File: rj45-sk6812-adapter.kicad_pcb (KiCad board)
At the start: 2 copper layers, 34.3 x 46.2 mm, 21 parts, among them J1 TE-Connectivity-406549-6, J2 Conn_01x05, J3 Conn_01x03, J4 Conn_01x03, J5 Conn_01x03, J6 Conn_01x03, J7 USB_B_Mini, J8 Screw_Terminal_01x02, Q1 2N7002, U1 L78L05_TO92

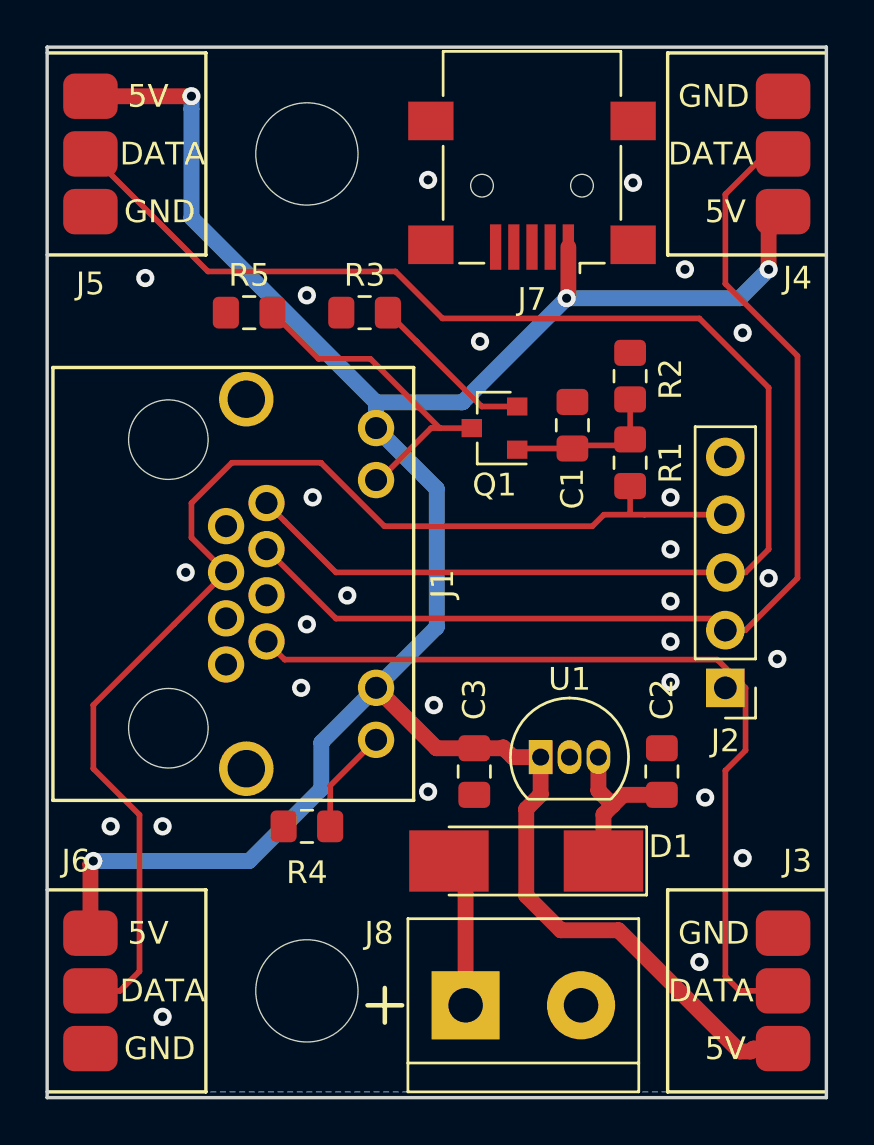
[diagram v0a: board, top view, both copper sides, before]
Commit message: Added capacitor to stabilize the LEDs' 5V supply
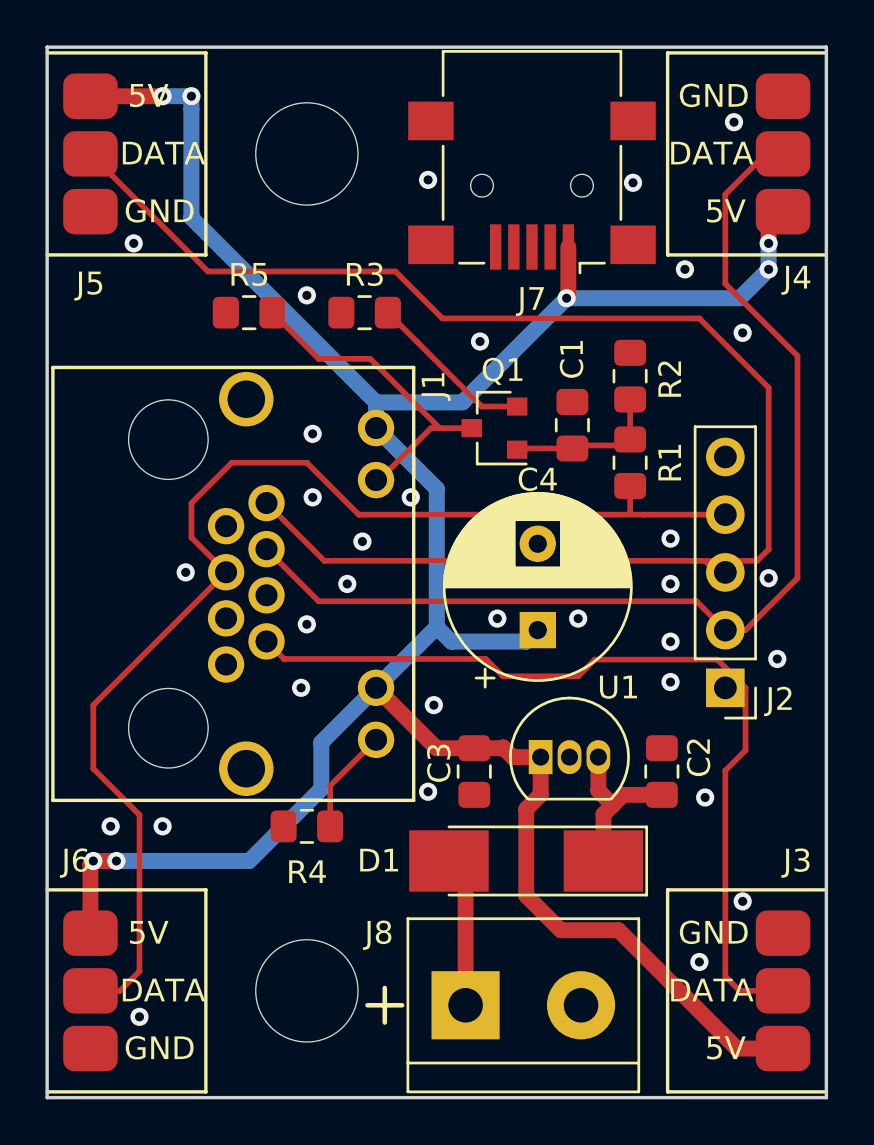
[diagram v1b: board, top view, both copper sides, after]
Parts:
- added C4: 100uF, Capacitor_THT:CP_Radial_D8.0mm_P3.80mm, F.Cu at (148.6, 82.5)
- C2, C3: value 22uF -> 100nF
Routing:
- net +5V: track 110.0 -> 115.8 mm, vias 4 -> 7
- net /DATA3: track 65.0 -> 66.3 mm
- net /DATA1: track 37.8 -> 38.5 mm
- net GND: vias 27 -> 32
